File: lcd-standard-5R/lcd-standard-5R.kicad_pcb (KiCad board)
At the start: 2 copper layers, 137.4 x 82.6 mm, 101 parts, among them J1 SWD, J2 Conn_01x40_MountingPin, J3 Micro_SD_Card_Det1, J4 USB_C_Receptacle_USB2.0_16P, J5 Conn_01x06_MountingPin, J6 Serial, J7 Conn_ARM_JTAG_SWD_10, J8 Conn_01x12_MountingPin, Q1 DMG2301L, Q2 MMBT3904, SW1 BOOT0, SW2 RST, U1 siplex-som-s16, U2 TPS61169, U3 XPT2046TS, U4 CAT24C256, U5 AMS1117-3.3

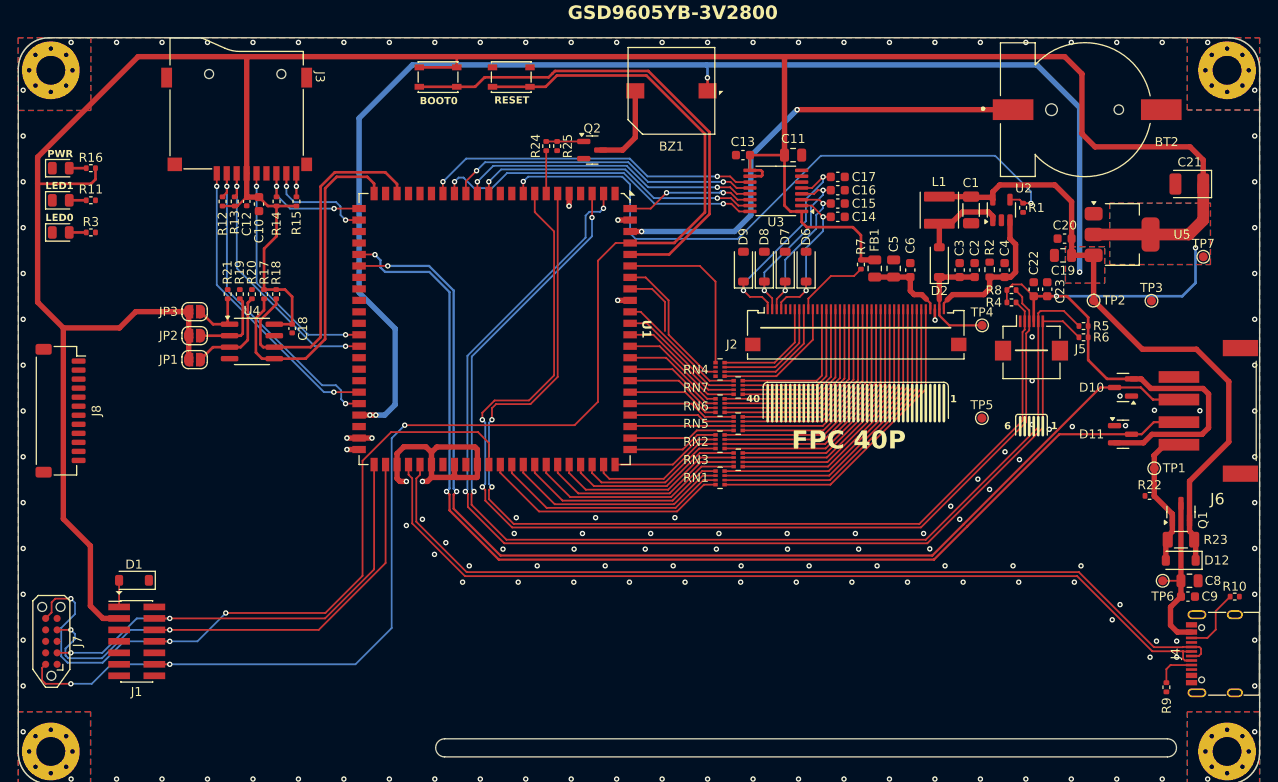
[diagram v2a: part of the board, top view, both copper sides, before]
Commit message: Adding MAX98357 I2S mono Amplifier
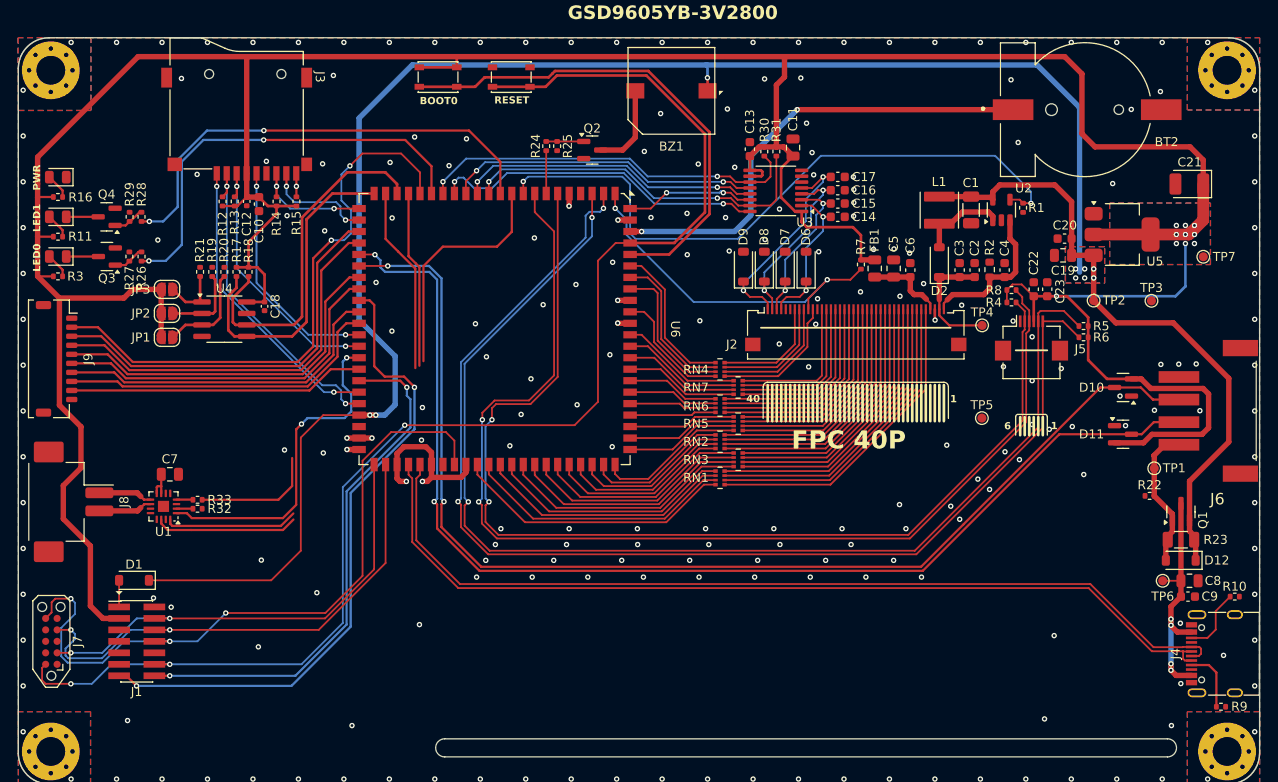
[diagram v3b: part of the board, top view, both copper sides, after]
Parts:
- added C7: 10u, Capacitor_SMD:C_0805_2012Metric, F.Cu at (93.2, 102.2)
- added J9: Conn_01x10_MountingPin, Connector_JST:JST_SHL_SM10B-SHLS-TF_1x10-1MP_P1.00mm_Horizontal, F.Cu at (80.7, 89.5)
- added Q3: MMBT3904, Package_TO_SOT_SMD:SOT-23, F.Cu at (86.2, 78.1)
- added Q4: MMBT3904, Package_TO_SOT_SMD:SOT-23, F.Cu at (86.2, 73.7)
- added R26: 1K, Resistor_SMD:R_0402_1005Metric, F.Cu at (90.1, 78.1)
- added R27: 10K, Resistor_SMD:R_0402_1005Metric, F.Cu at (88.7, 78.1)
- added R28: 1K, Resistor_SMD:R_0402_1005Metric, F.Cu at (90.1, 73.7)
- added R29: 10K, Resistor_SMD:R_0402_1005Metric, F.Cu at (88.7, 73.7)
- added R30: 10K, Resistor_SMD:R_0402_1005Metric, F.Cu at (159.0, 66.5)
- added R31: 10K, Resistor_SMD:R_0402_1005Metric, F.Cu at (160.3, 66.5)
- added R32: 100K, Resistor_SMD:R_0402_1005Metric, F.Cu at (96.3, 106.0)
- added R33: 1M, Resistor_SMD:R_0402_1005Metric, F.Cu at (96.3, 105.1)
- added U6: siplex-som-s16, siplex:siplex-som-s16, F.Cu at (129.1, 86.2)
- J8: value Conn_01x12_MountingPin -> Conn_01x02_MountingPin; footprint Connector_JST:JST_SH_SM12B-SRSS-TB_1x12-1MP_P1.00mm_Horizontal -> Connector_Hirose:Hirose_DF3EA-02P-2H_1x02-1MP_P2.00mm_Horizontal
- R2: value 6.8R -> 4.7R
- RN1, RN2, RN3, RN4, RN5, RN6, RN7: value 22 -> 100
- U1: value siplex-som-s16 -> MAX98357A; footprint siplex:siplex-som-s16 -> Package_DFN_QFN:TQFN-16-1EP_3x3mm_P0.5mm_EP1.23x1.23mm
- moved U1 41.6 mm to (92.5, 105.8), turned to 180 degrees
- moved J8 10.2 mm to (82.5, 105.3)
- moved R9 6.42 mm to (209.6, 128.0), turned to 180 degrees
- moved R3 6.07 mm to (80.8, 80.3)
- moved R11 5.43 mm to (80.8, 75.9)
- moved R16 4.84 mm to (80.8, 71.5), turned to 0 degrees
- moved JP1 3.92 mm to (92.9, 87.1)
- moved JP2 3.92 mm to (92.9, 84.4)
- moved R17 3.92 mm to (100.6, 79.8)
- moved R18 3.92 mm to (101.9, 79.8)
- moved R20 3.92 mm to (99.2, 79.8)
- moved R21 3.92 mm to (96.5, 79.8)
- moved U4 3.92 mm to (99.2, 85.1)
- moved C18 3.92 mm to (103.7, 83.6)
- moved JP3 3.92 mm to (92.9, 81.8)
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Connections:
- D3 pad 1: GND -> Net-(D3-K)
- D4 pad 1: GND -> Net-(D4-K)
- J1 pad 13: /VCP_RX -> /DBG_RX
- J1 pad 14: /VCP_TX -> /DBG_TX
- J8 pad 1: unconnected-(J8-Pin_1-Pad1) -> Net-(J8-Pin_1)
- J8 pad 2: unconnected-(J8-Pin_2-Pad2) -> Net-(J8-Pin_2)
- R11 pad 1: /LED1 -> Net-(D4-A)
- R11 pad 2: Net-(D4-A) -> +3V3
- R3 pad 1: /LED0 -> Net-(D3-A)
- R3 pad 2: Net-(D3-A) -> +3V3
- U1 pad 1: unconnected-(U1-PB7-Pad1) -> /I2S2_SDO
- U1 pad 10: unconnected-(U1-PA1-Pad10) -> Net-(J8-Pin_2)
- U1 pad 11: unconnected-(U1-PA4-Pad11) -> GND
- U1 pad 12: /TP_CS -> unconnected-(U1-NC-Pad12)
- U1 pad 13: /TP_BUSY -> unconnected-(U1-NC-Pad13)
- U1 pad 14: /TP_MISO -> /I2S2_WS
- U1 pad 15: /TP_CLK -> GND
- U1 pad 16: /TP_IRQ -> /I2S2_CLK
- U1 pad 17: unconnected-(U1-PB1-Pad17) -> GND
- U1 pad 2: /TP_SCL -> /GAIN_SLOT
- U1 pad 3: /TP_SDA -> GND
- U1 pad 4: unconnected-(U1-PH4-Pad4) -> Net-(U1-~{SD_MODE})
- U1 pad 5: GND -> unconnected-(U1-NC-Pad5)
- U1 pad 6: /TP_INT -> unconnected-(U1-NC-Pad6)
- U1 pad 7: /BUZZER -> VDD
- U1 pad 8: /TP_WAKE -> VDD
- U1 pad 9: /LCD_BLK -> Net-(J8-Pin_1)
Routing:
- net /DBG_RX: track 0.00 -> 72.3 mm, vias 0 -> 2
- net /IO_7: track 0.00 -> 63.9 mm, vias 0 -> 2
- net /DBG_TX: track 0.00 -> 58.6 mm, vias 0 -> 2
- net /LED1: track 0.00 -> 51.9 mm, vias 0 -> 2
- net /LED0: track 0.00 -> 47.3 mm, vias 0 -> 2
- net /IO_6: track 0.00 -> 44.9 mm
- net /IO_5: track 0.00 -> 43.9 mm
- net VDD: track 214.5 -> 256.2 mm, vias 4 -> 9
- net /IO_4: track 0.00 -> 40.4 mm
- net /~{SD_MODE}: track 0.00 -> 39.8 mm
- net /IO_3: track 0.00 -> 39.4 mm
- net /IO_2: track 0.00 -> 37.5 mm
- net /I2S2_SDO: track 0.00 -> 37.2 mm, vias 0 -> 2
- net /IO_1: track 0.00 -> 36.5 mm
- net /I2S2_CLK: track 0.00 -> 35.5 mm
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
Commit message: LCD 5inch, finished tracks, LCD square, Adding MAX98357A
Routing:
- net /I2S2_WS: track 35.4 -> 59.0 mm, vias 0 -> 2
- net VDD: track 256.2 -> 279.2 mm
- net /I2S2_CLK: track 35.5 -> 57.9 mm, vias 0 -> 2
- net /~{SD_MODE}: track 39.8 -> 59.0 mm, vias 0 -> 2
- net /DBG_RX: track 72.3 -> 73.7 mm
- net /DBG_TX: track 58.6 -> 59.4 mm
- net GND: vias 229 -> 249
- net (no net): vias 0 -> 1

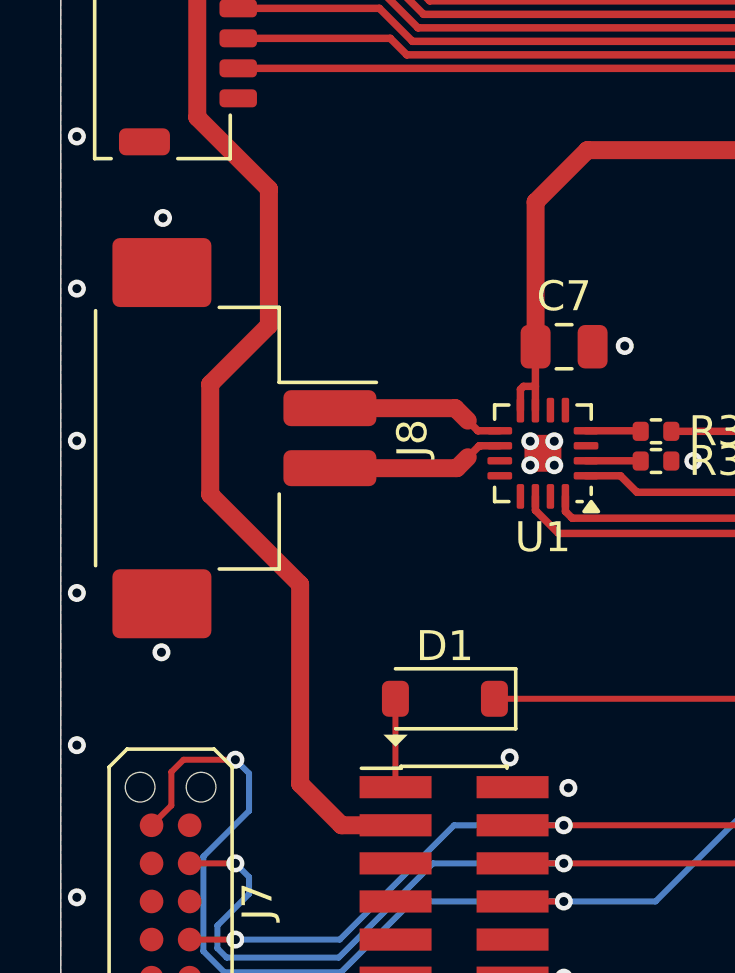
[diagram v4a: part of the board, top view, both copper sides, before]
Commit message: Add LCD standard 7inch
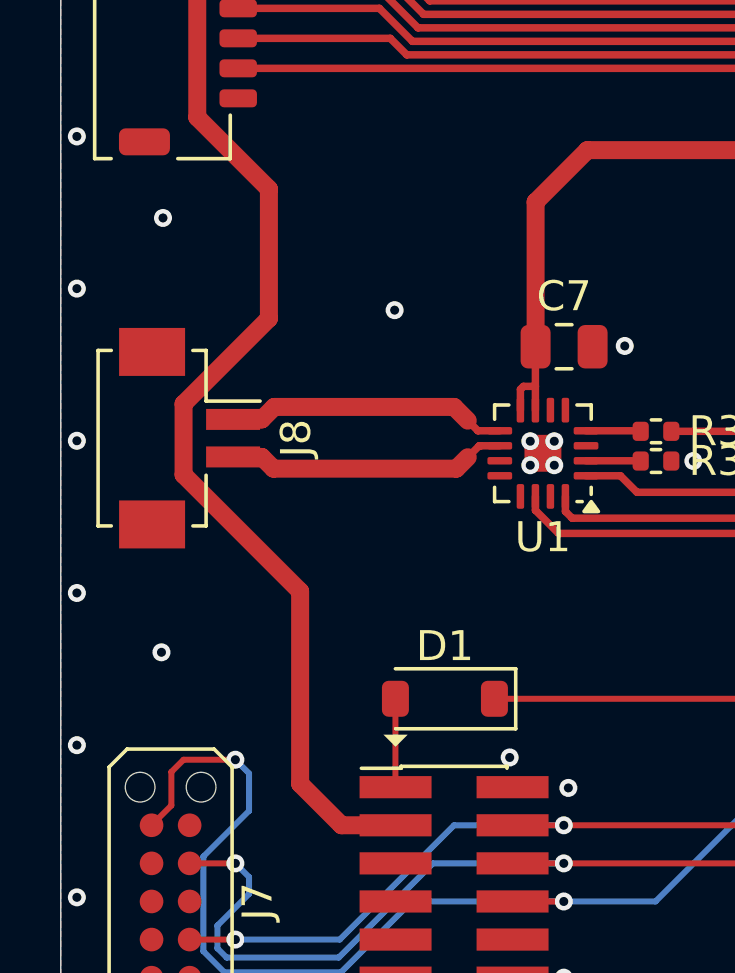
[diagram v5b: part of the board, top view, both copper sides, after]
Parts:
- J8: footprint Connector_Hirose:Hirose_DF3EA-02P-2H_1x02-1MP_P2.00mm_Horizontal -> Connector_Hirose:Hirose_DF13C_CL535-0402-2-51_1x02-1MP_P1.25mm_Vertical
- moved J8 1.83 mm to (80.7, 105.3)
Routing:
- net Net-(J8-Pin_1): track 5.97 -> 9.39 mm
- net Net-(J8-Pin_2): track 5.97 -> 9.37 mm
- net +3V3: track 398.3 -> 399.0 mm
- net GND: vias 249 -> 250
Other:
- board text added: "SPEAKER"

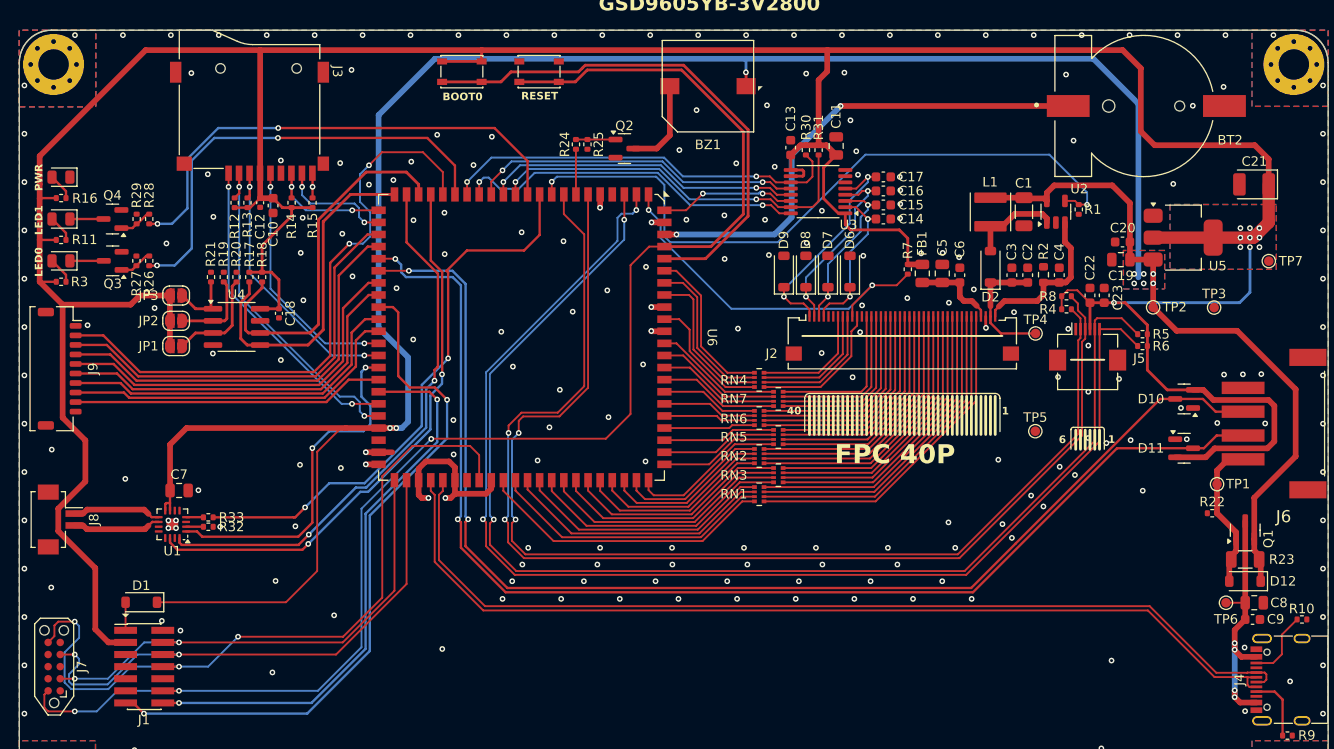
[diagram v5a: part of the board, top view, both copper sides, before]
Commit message: Added sd_det tracks
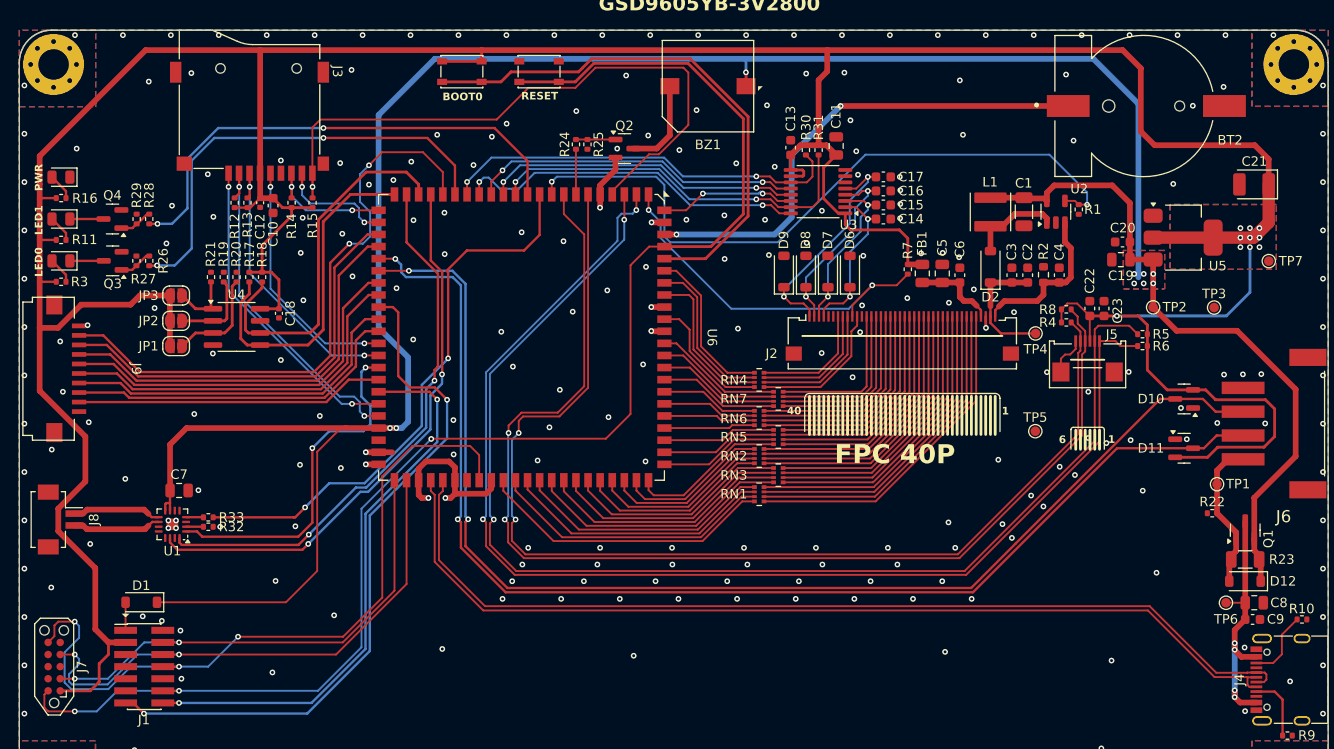
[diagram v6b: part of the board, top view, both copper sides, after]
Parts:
- J5: footprint Connector_FFC-FPC:Hirose_FH12-6S-0.5SH_1x06-1MP_P0.50mm_Horizontal -> Connector_FPC:Conn_FPC_6P_0.5mm_XUNPU_FPC-05FB-6PH20
- J9: footprint Connector_JST:JST_SHL_SM10B-SHLS-TF_1x10-1MP_P1.00mm_Horizontal -> Connector_FPC:Conn_FPC_10P_1mm_G-SWITCH_GT-F1008SR20-10SMT01
- RN1, RN2, RN3, RN4, RN5, RN6, RN7: value 100 -> 50
- moved J9 2.04 mm to (82.7, 89.5)
- moved C22 1.38 mm to (188.8, 83.1)
- moved C23 1.38 mm to (190.3, 83.1)
- moved R4 1.38 mm to (186.3, 84.6)
- moved R8 1.38 mm to (186.3, 83.2)
- moved J5 0.60 mm to (188.6, 86.5)
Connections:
- J7 pad 1: unconnected-(J7-VTref-Pad1) -> +3V3
- U6 pad 4: unconnected-(U6-PH4-Pad4) -> /SD_DET
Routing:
- net /SD_DET: track 2.59 -> 66.4 mm
- net +3V3: track 399.0 -> 410.6 mm
- net GND: track 28.3 -> 37.1 mm, vias 250 -> 269
- net /TP_SCL: track 132.4 -> 130.6 mm
- net /TP_WAKE: track 124.9 -> 123.5 mm
- net /TP_INT: track 121.1 -> 119.7 mm
- net /BOOT0: track 55.4 -> 56.7 mm
- net /RESET: track 151.8 -> 153.2 mm
- net /TP_SDA: track 131.2 -> 130.0 mm

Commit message: Slight changes
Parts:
- C1: value 10u -> 10u/1206
- C13, C14, C15, C16, C17, C20, C23, C4, C6, C9: footprint Capacitor_SMD:C_0603_1608Metric -> Capacitor_SMD:C_0402_1005Metric
- C21: footprint Capacitor_Tantalum_SMD:CP_EIA-3528-12_Kemet-T -> Capacitor_Tantalum_SMD:CP_EIA-3216-18_Kemet-A
- moved R2 1.73 mm to (185.7, 79.6)
- moved C4 1.63 mm to (184.0, 79.9)
- moved C23 1.51 mm to (188.8, 83.4)
- moved C22 1.37 mm to (190.2, 83.1)
- moved C20 0.30 mm to (192.5, 76.1)
- moved C9 0.30 mm to (205.6, 115.8)
- moved C13 0.30 mm to (157.4, 66.5)
- moved C6 0.30 mm to (175.2, 79.9)
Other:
- board text added: "NEXTRON8048X050"
